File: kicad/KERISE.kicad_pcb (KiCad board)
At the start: 2 copper layers, 47 x 50 mm, 119 parts, among them J1 USB_OTG, P1 ANT, P10 Partition, P11 PR_Host, P12 PR_Slave, P13 Partition, P14 Partition, P15 Partition, P16 Partition, P17 COM, P18 Fan, P19 ENC_Host, P2 Motor_L, P20 ENC_Slave, P21 ToF_Host, P22 ToF_Slave, P23 COM, P24 ENC_Host, P25 ENC_Slave, P3 Motor_R, P4 Battery, P5 PR_Host, P6 PR_Slave, P7 Partition, P8 Partition, P9 Partition, Q1 IRFML8244, Q2 IRFML8244, Q3 IRFML8244, Q4 IRFML8244, SW1 SW_Push, SW2 SW_Push, U1 FLASH, U10 MCP73831, U11 FT234XD, U12 AS5048A, U13 ICM-20602, U14 FLASH, U15 FLASH, U2 ESP32, U3 XTAL, U4 DRV8835, U5 LXDC2URxx, U6 AD8601, U7 AD8601, U8 AS5048A, U9 VL53L0X

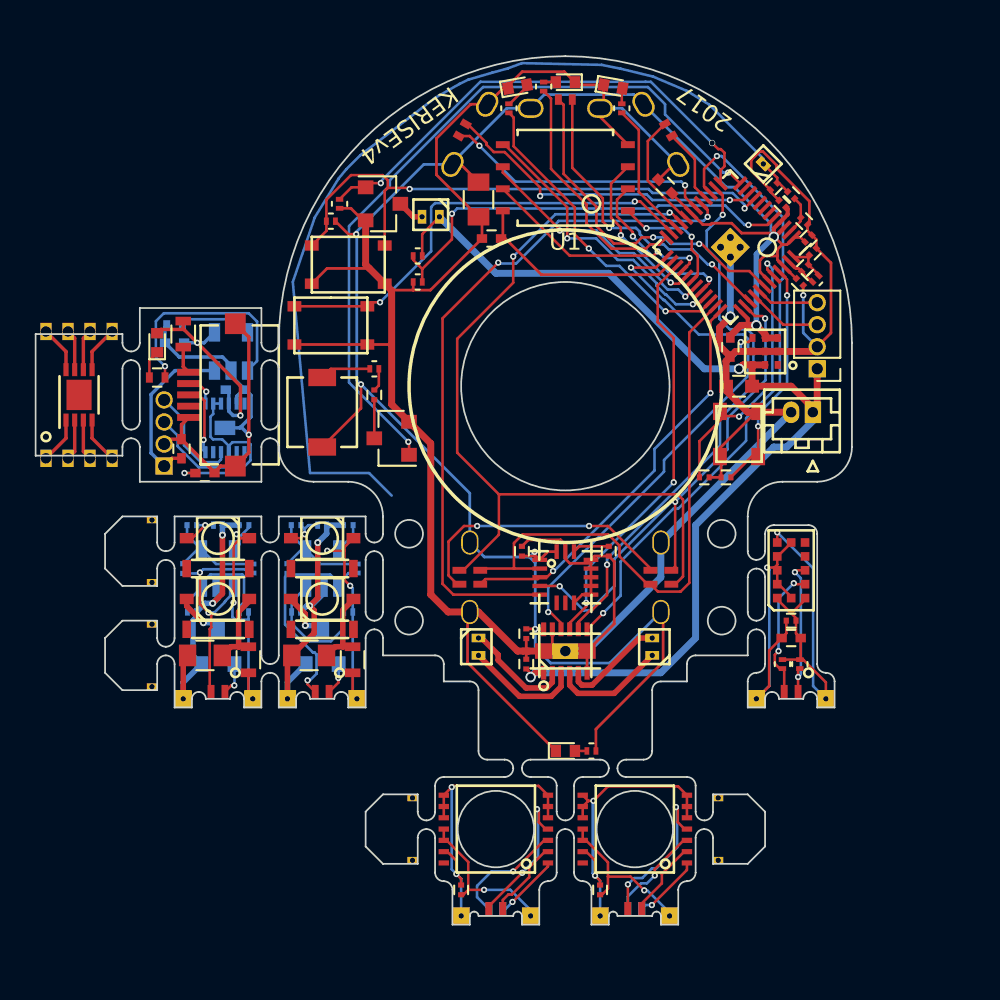
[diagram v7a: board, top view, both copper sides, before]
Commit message: 4輪の改良版を設計
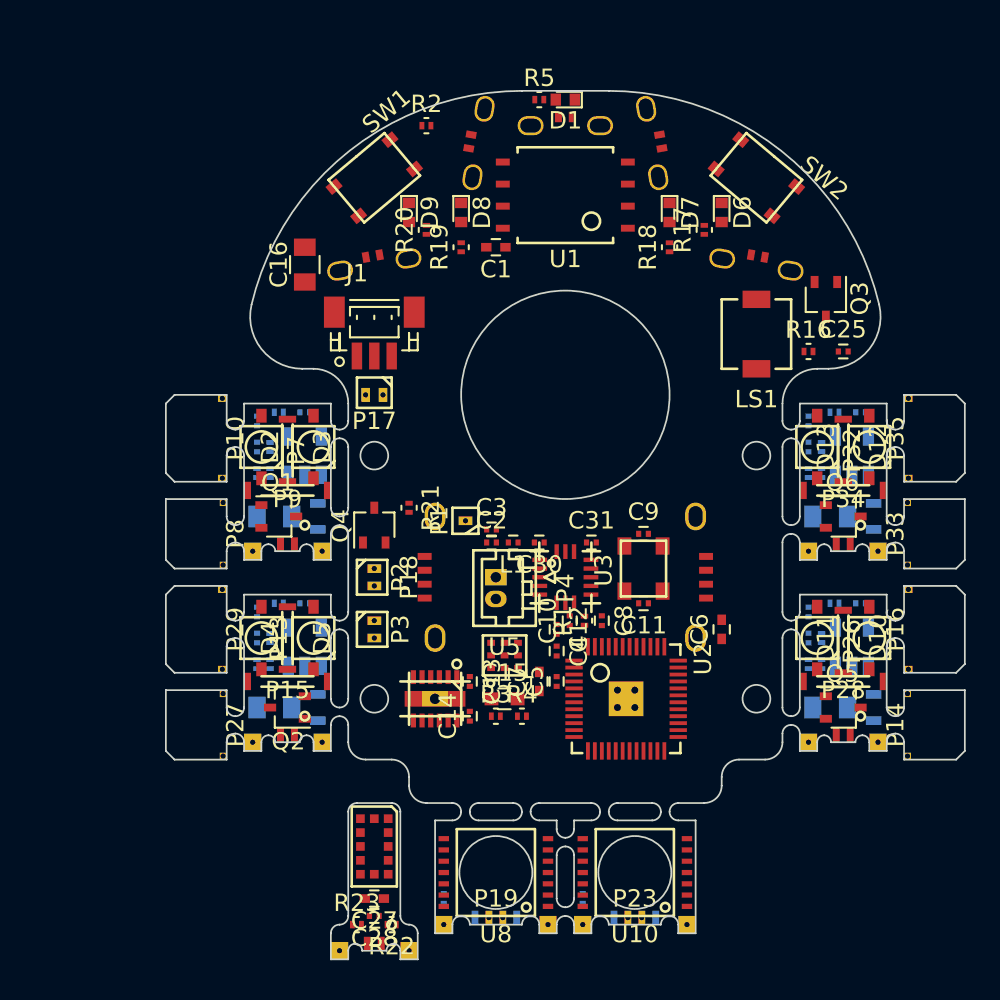
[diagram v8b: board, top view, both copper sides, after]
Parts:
- removed F1: FEMTOSMDC035F-02, Resistors_SMD:R_0603
- removed G***: LOGO, mouse:KERI_9mm
- removed the P17 at (163.0, 101.0)
- removed the R21 at (162.0, 118.0)
- removed U14: FLASH, Housings_DFN_QFN:DFN-8-1EP_3x2mm_Pitch0.5mm
- removed U15: FLASH, mouse:SOIJ-8_5.3x5.3mm_Pitch1.27mm_th
- added C36: 47u, Capacitors_SMD:C_0805, B.Cu at (163.8, 109.5)
- added C37: 0.01u, Capacitors_SMD:C_0201, B.Cu at (162.5, 104.0)
- added C38: 22p, Capacitors_SMD:C_0201, B.Cu at (162.5, 105.5)
- added C39: 0.1u, Capacitors_SMD:C_0201, B.Cu at (165.5, 103.5)
- added D10: VSMB294008G, mouse:VISHAY_DIODE, F.Cu at (166.0, 116.5)
- added D11: VEMD2020X01, mouse:VISHAY_DIODE, F.Cu at (163.0, 116.5)
- added D12: VSMB294008G, mouse:VISHAY_DIODE, F.Cu at (166.0, 105.5)
- added D13: VEMD2020X01, mouse:VISHAY_DIODE, F.Cu at (163.0, 105.5)
- added P18: ENC_Host, mouse:STAND_AS_HOST, F.Cu at (141.0, 113.0)
- added P26: Partition, mouse:Partition_Host, F.Cu at (164.5, 116.7)
- added P27: Partition, mouse:Partition_Slave, F.Cu at (129.0, 121.5)
- added P28: Partition, mouse:Partition_Long_Host, F.Cu at (164.5, 119.0)
- added P29: Partition, mouse:Partition_long_Slave, F.Cu at (129.0, 116.0)
- added P30: PR_Host, mouse:STAND_PR_HOST, F.Cu at (159.5, 95.0)
- added P31: PR_Slave, mouse:STAND_PR_SLAVE, F.Cu at (164.5, 111.5)
- added P32: Partition, mouse:Partition_Host, F.Cu at (164.5, 105.7)
- added P33: Partition, mouse:Partition_Slave, F.Cu at (168.0, 110.5)
- added P34: Partition, mouse:Partition_Long_Host, F.Cu at (164.5, 108.0)
- added P35: Partition, mouse:Partition_long_Slave, F.Cu at (168.0, 105.0)
- added Q5: DMN3065LW-7, TO_SOT_Packages_SMD:SOT-323_SC-70, F.Cu at (164.5, 120.5)
- added Q6: DMN3065LW-7, TO_SOT_Packages_SMD:SOT-323_SC-70, F.Cu at (164.5, 109.5)
- added R20: 1k, Resistors_SMD:R_0201, F.Cu at (140.5, 93.0)
- added R25: 100k, Resistors_SMD:R_0201, B.Cu at (164.0, 114.5)
- added R26: 1k, Resistors_SMD:R_0201, B.Cu at (162.5, 118.0)
- added R27: 1k, Resistors_SMD:R_0201, B.Cu at (163.2, 118.0)
- added R28: 220k, Resistors_SMD:R_0201, B.Cu at (163.2, 116.5)
- added R29: 47, Resistors_SMD:R_0603, B.Cu at (166.2, 109.5)
- added R30: 100k, Resistors_SMD:R_0201, B.Cu at (164.0, 103.5)
- added R31: 1k, Resistors_SMD:R_0201, B.Cu at (162.5, 107.0)
- added R32: 1k, Resistors_SMD:R_0201, B.Cu at (163.2, 107.0)
- added R33: 220k, Resistors_SMD:R_0201, B.Cu at (163.2, 105.5)
- C17, C21, C26, C35, R11, R6: moved to B.Cu
- C29, C31: footprint Capacitors_SMD:C_0402 -> Capacitors_SMD:C_0201
- C30: value 4.7u -> 0.1u; footprint Capacitors_SMD:C_0402 -> Capacitors_SMD:C_0201; moved to F.Cu
- C32: value 4.7u -> 47u; footprint Capacitors_SMD:C_0402 -> Capacitors_SMD:C_0805; moved to B.Cu
- C33: value 0.1u -> 0.01u; moved to B.Cu
- C34: value 0.1u -> 22p; moved to B.Cu
- D9: value Status -> LED
- J1: value USB_OTG -> COM; footprint mouse:ZX62R-B-5P -> Connectors_JST:JST_SH_BM03B-SRSS-TB_03x1.00mm_Straight
- P10, P16: footprint mouse:Partition_Slave -> mouse:Partition_long_Slave
- P15, P9: footprint mouse:Partition_Host -> mouse:Partition_Long_Host
- P19: value ENC_Host -> ENC_Slave; footprint mouse:STAND_AS_HOST -> mouse:STAND_AS_SLAVE
- P20: value ENC_Slave -> ToF_Host; footprint mouse:STAND_AS_SLAVE -> mouse:STAND_PR_HOST; moved to F.Cu
- P21: value ToF_Host -> ToF_Slave; footprint mouse:STAND_PR_HOST -> mouse:STAND_PR_SLAVE
- P22: value ToF_Slave -> ENC_Host; footprint mouse:STAND_PR_SLAVE -> mouse:STAND_AS_HOST
- P23: value COM -> ENC_Slave; footprint Socket_Strips:Socket_Strip_Straight_1x04_Pitch1.27mm -> mouse:STAND_AS_SLAVE; moved to F.Cu
- P24: value ENC_Host -> PR_Host; footprint mouse:STAND_AS_HOST -> mouse:STAND_PR_HOST
- P25: value ENC_Slave -> PR_Slave; footprint mouse:STAND_AS_SLAVE -> mouse:STAND_PR_SLAVE; moved to F.Cu
- Q1, Q2: value IRFML8244 -> DMN3065LW-7; footprint TO_SOT_Packages_SMD:SOT-23 -> TO_SOT_Packages_SMD:SOT-323_SC-70; moved to F.Cu
- Q3: value IRFML8244 -> NX3020NAKW; footprint TO_SOT_Packages_SMD:SOT-23 -> TO_SOT_Packages_SMD:SOT-323_SC-70
- Q4: value IRFML8244 -> DMN3065LW-7; footprint TO_SOT_Packages_SMD:SOT-23 -> TO_SOT_Packages_SMD:SOT-323_SC-70
- R23: footprint Resistors_SMD:R_0402 -> Resistors_SMD:R_0201; moved to F.Cu
- R24: value 10k -> 47; footprint Resistors_SMD:R_0402 -> Resistors_SMD:R_0603; moved to B.Cu
- U10: value MCP73831 -> AS5048A; footprint TO_SOT_Packages_SMD:SOT-23-5 -> mouse:TSSOP-14_4.4x5mm_Pitch0.65mm; moved to F.Cu
- U11: value FT234XD -> ICM-20602; footprint mouse:DFN-12-1EP_3x3mm_Pitch0.45mm -> mouse:LGA-16-3x3; moved to F.Cu
- U12: value AS5048A -> AD8601; footprint mouse:TSSOP-14_4.4x5mm_Pitch0.65mm -> TO_SOT_Packages_SMD:SOT-23-5; moved to B.Cu
- U13: value ICM-20602 -> AD8601; footprint mouse:LGA-16-3x3 -> TO_SOT_Packages_SMD:SOT-23-5; moved to B.Cu
- moved P21 49.7 mm to (137.5, 134.5), turned to 180 degrees
- moved P20 45.7 mm to (148.5, 87.0), turned to 0 degrees
- moved R24 45.4 mm to (166.2, 120.5), turned to 90 degrees
- moved C32 40.2 mm to (163.8, 120.5), turned to 180 degrees
- moved U10 38.0 mm to (152.5, 130.0), turned to 180 degrees
- moved P23 37.8 mm to (152.5, 133.0)
- moved R5 37.6 mm to (147.0, 85.5), turned to 0 degrees
- moved D1 37.5 mm to (148.5, 85.5), turned to 180 degrees
- moved R23 36.1 mm to (136.5, 133.0), turned to 0 degrees
- moved C29 35.5 mm to (149.5, 131.5), turned to 90 degrees
- moved C5 30.4 mm to (148.0, 119.0), turned to 90 degrees
- moved C28 29.4 mm to (137.5, 132.5)
- moved C7 29.4 mm to (147.0, 119.0), turned to 90 degrees
- moved U9 28.8 mm to (137.5, 128.5), turned to 90 degrees
- moved P14 28.6 mm to (168.0, 121.5), turned to 270 degrees
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- renumbered P18 to P17, R20 to R21
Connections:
- net PR-LED-L renamed PR-LED-SL
- C29 pad 1: /Writer/USB_5V -> /Encoder_L/s_VDD
- C29 pad 2: /Writer/USB_GND -> /Encoder_L/s_GND
- C30 pad 1: /Writer/USB_5V -> +3V3
- C30 pad 2: /Writer/USB_GND -> GND
- C31 pad 2: /Writer/USB_GND -> GND
- C32 pad 1: /Writer/BAT_OUT -> /IR_RCV_FL/LED_to_C
- C32 pad 2: /Writer/USB_GND -> /IR_RCV_FL/s_GND
- C33 pad 1: /Encoder_L/s_VDD -> Net-(C33-Pad1)
- C33 pad 2: /Encoder_L/s_GND -> Net-(C33-Pad2)
- C34 pad 1: +3V3 -> /IR_RCV_FL/s_IR_RCV
- C34 pad 2: GND -> Net-(C33-Pad1)
- C35 pad 1: Net-(C35-Pad1) -> /IR_RCV_FL/s_3.3V
- C35 pad 2: GND -> /IR_RCV_FL/s_GND
- D9 pad 1: Net-(D9-Pad1) -> GND
- D9 pad 2: /Writer/USB_5V -> Net-(D9-Pad2)
- J1 pad 1: /Writer/USB_BUS -> GND
- J1 pad 2: /Writer/USB_D- -> UART-RX
- J1 pad 3: /Writer/USB_D+ -> UART-TX
- P11 pad 2: PR-LED-R -> PR-LED-SR
- P11 pad 3: PR-RCV-R -> PR-RCV-SR
- P19 pad 1: +3V3 -> /Encoder_R/s_VDD
- P19 pad 2: SPI-CS-ENC -> /Encoder_R/s_CS
- P19 pad 3: SPI-SCLK -> /Encoder_R/s_SCLK
- P19 pad 4: ENC-CHAIN -> /Encoder_R/s_MISO
- P19 pad 5: SPI-MOSI -> /Encoder_R/s_MOSI
- P19 pad 6: GND -> /Encoder_R/s_GND
- P20 pad 1: /Encoder_R/s_VDD -> +3V3
- P20 pad 2: /Encoder_R/s_CS -> I2C-SDA
- P20 pad 3: /Encoder_R/s_SCLK -> I2C-SCL
- P20 pad 4: /Encoder_R/s_MISO -> GND
- P21 pad 1: +3V3 -> /ToF/s_3.3V
- P21 pad 2: I2C-SDA -> /ToF/s_SDA
- P21 pad 3: I2C-SCL -> /ToF/s_SCL
- P21 pad 4: GND -> /ToF/s_GND
- P22 pad 1: /ToF/s_3.3V -> +3V3
- P22 pad 2: /ToF/s_SDA -> SPI-CS-ENC
- P22 pad 3: /ToF/s_SCL -> SPI-SCLK
- P22 pad 4: /ToF/s_GND -> SPI-MISO
- P23 pad 1: /Writer/BAT_OUT -> /Encoder_L/s_VDD
- P23 pad 2: /Writer/USB_GND -> /Encoder_L/s_CS
- P23 pad 3: /Writer/USB_TX -> /Encoder_L/s_SCLK
- P23 pad 4: /Writer/USB_RX -> /Encoder_L/s_MISO
- P24 pad 2: SPI-CS-ENC -> PR-LED-SR
- P24 pad 3: SPI-SCLK -> PR-RCV-FL
- P24 pad 4: SPI-MISO -> GND
- P25 pad 1: /Encoder_L/s_VDD -> /IR_RCV_FL/s_3.3V
- P25 pad 2: /Encoder_L/s_CS -> /IR_RCV_FL/s_IR_LED
- P25 pad 3: /Encoder_L/s_SCLK -> /IR_RCV_FL/s_IR_RCV
- P25 pad 4: /Encoder_L/s_MISO -> /IR_RCV_FL/s_GND
- P5 pad 3: PR-RCV-L -> PR-RCV-SL
- R22 pad 2: /ToF/s_SCL -> /ToF/s_SDA
- R23 pad 1: Net-(R23-Pad1) -> /ToF/s_3.3V
- R23 pad 2: /Writer/USB_GND -> /ToF/s_SCL
- R24 pad 1: Net-(D9-Pad1) -> /IR_RCV_FL/s_3.3V
- R24 pad 2: Net-(R24-Pad2) -> /IR_RCV_FL/LED_to_C
- U10 pad 1: Net-(R24-Pad2) -> /Encoder_L/s_CS
- U10 pad 2: /Writer/USB_GND -> /Encoder_L/s_SCLK
- U10 pad 3: /Writer/BAT_OUT -> /Encoder_L/s_MISO
- U10 pad 4: /Writer/USB_5V -> /Encoder_L/s_MOSI
- U10 pad 5: Net-(R23-Pad1) -> /Encoder_L/s_GND
- U11 pad 1: /Writer/USB_D- -> +3V3
- U11 pad 10: /Writer/USB_RX -> GND
- U11 pad 11: (no net) -> GND
- U11 pad 12: /Writer/USB_D+ -> GND
- U11 pad 13: /Writer/USB_GND -> GND
- U11 pad 2: Net-(C31-Pad1) -> SPI-SCLK
- U11 pad 3: Net-(C31-Pad1) -> SPI-MOSI
- U11 pad 4: /Writer/USB_5V -> SPI-MISO
- U11 pad 5: /Writer/USB_GND -> SPI-CS-AXIS
- U11 pad 7: /Writer/USB_TX -> (no net)
- U11 pad 8: (no net) -> GND
- U11 pad 9: Net-(C31-Pad1) -> GND
- U12 pad 1: /Encoder_L/s_CS -> /IR_RCV_FL/s_IR_RCV
- U12 pad 2: /Encoder_L/s_SCLK -> /IR_RCV_FL/s_GND
- U12 pad 3: /Encoder_L/s_MISO -> Net-(R26-Pad2)
- U12 pad 4: /Encoder_L/s_MOSI -> Net-(C33-Pad1)
- U12 pad 5: /Encoder_L/s_GND -> /IR_RCV_FL/s_3.3V
- U13 pad 1: +3V3 -> /IR_RCV_FR/s_IR_RCV
- U13 pad 2: SPI-SCLK -> /IR_RCV_FR/s_GND
- U13 pad 3: SPI-MOSI -> Net-(R31-Pad2)
- U13 pad 4: SPI-MISO -> Net-(C37-Pad1)
- U13 pad 5: SPI-CS-AXIS -> /IR_RCV_FR/s_3.3V
- U2 pad 10: PR-RCV-L -> (no net)
- U2 pad 11: (no net) -> BAT-VOL
- U2 pad 16: PR-RCV-R -> LED_4
- U2 pad 20: PR-LED-R -> PR-LED-SR
- U2 pad 5: BAT-VOL -> PR-RCV-SL
- U2 pad 6: (no net) -> PR-RCV-SR
- U2 pad 7: (no net) -> PR-RCV-FL
- U2 pad 8: (no net) -> PR-RCV-FR
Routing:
- net GND: track 177.7 -> 0.00 mm, vias 2 -> 0
- net +3V3: track 119.1 -> 0.00 mm, vias 6 -> 0
- net +BATT: track 64.0 -> 0.00 mm, vias 3 -> 0
- net Net-(C2-Pad1): track 53.7 -> 0.00 mm
- net SPI-CS-ENC: track 48.4 -> 0.00 mm, vias 2 -> 0
- net SPEAKER: track 43.2 -> 0.00 mm, vias 2 -> 0
- net SPI-CS-AXIS: track 39.8 -> 0.00 mm, vias 2 -> 0
- net MT-IN-R2: track 36.4 -> 0.00 mm, vias 2 -> 0
- net SPI-SCLK: track 33.7 -> 0.00 mm
- net Net-(R2-Pad1): track 33.1 -> 0.00 mm, vias 2 -> 0
- net MT-IN-L1: track 32.6 -> 0.00 mm, vias 2 -> 0
- net MT-IN-R1: track 31.9 -> 0.00 mm, vias 2 -> 0
- net SPI-MISO: track 30.1 -> 0.00 mm, vias 3 -> 0
- net FAN: track 28.6 -> 0.00 mm, vias 2 -> 0
- net /Writer/USB_GND: track 27.7 -> 0.00 mm, vias 1 -> 0
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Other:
- board size 47 x 50 mm -> 46 x 50 mm
- net class 3.3V: clearance 0.15 -> 0.16; trace_width 0.16 -> 0.238
- net class BATT: clearance 0.15 -> 0.16; trace_width 0.15 -> 0.32; via_dia 0.36 -> 0.38; via_drill 0.3 -> 0.32
- net class Charger removed
- net class Default: clearance 0.15 -> 0.16; trace_width 0.15 -> 0.16; via_dia 0.36 -> 0.34
- net class GND: clearance 0.15 -> 0.16; trace_width 0.16 -> 0.32; via_dia 0.36 -> 0.38; via_drill 0.3 -> 0.32
- net class LED: clearance 0.15 -> 0.16; trace_width 0.32 -> 0.24; via_dia 0.4 -> 0.36
- net class Motor: clearance 0.15 -> 0.16; trace_width 0.32 -> 0.3; via_dia 0.4 -> 0.36
- rule trace_clearance: 0.15 -> 0.16
- rule trace_min: 0.15 -> 0.16
- rule via_min_size: 0.3 -> 0.34
- board text removed: "2017"
- board text removed: "KERISEv4"
